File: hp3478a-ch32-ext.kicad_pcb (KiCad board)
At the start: 4 copper layers, 40 x 50 mm, 55 parts, among them J1 Conn_GPIB, J2 Pwr, J4 USB, J5 Micro_SD_Card_Det1, Q1 BSS138, SW1 RST, U1 CH32V203CxTx, U2 TLV76701DRVx, U3 AHT20, Y1 24MHz, 10pF

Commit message: chore: upd
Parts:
- R1: value 430k -> 470k
- R2: value 82k -> 150k

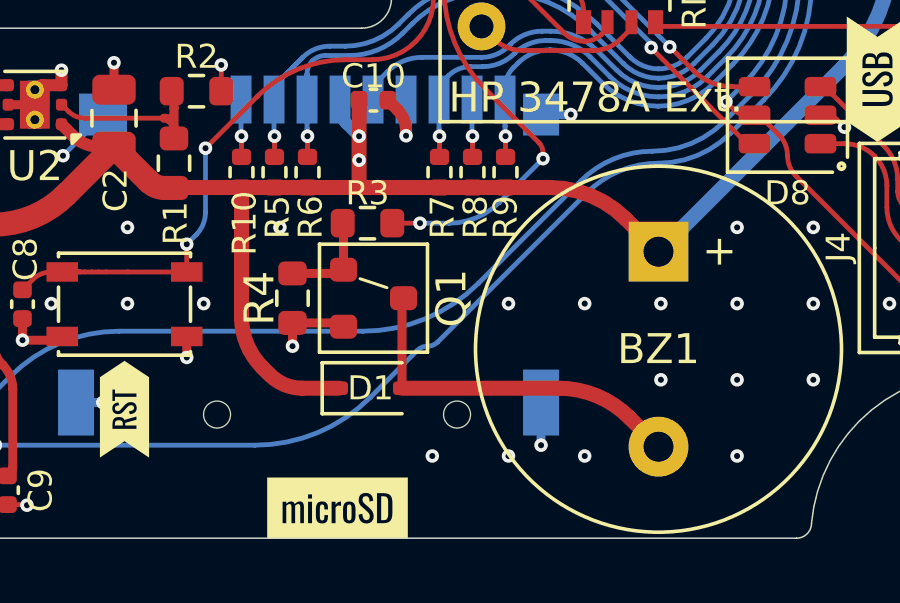
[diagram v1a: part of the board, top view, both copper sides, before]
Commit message: fix: hole clearance
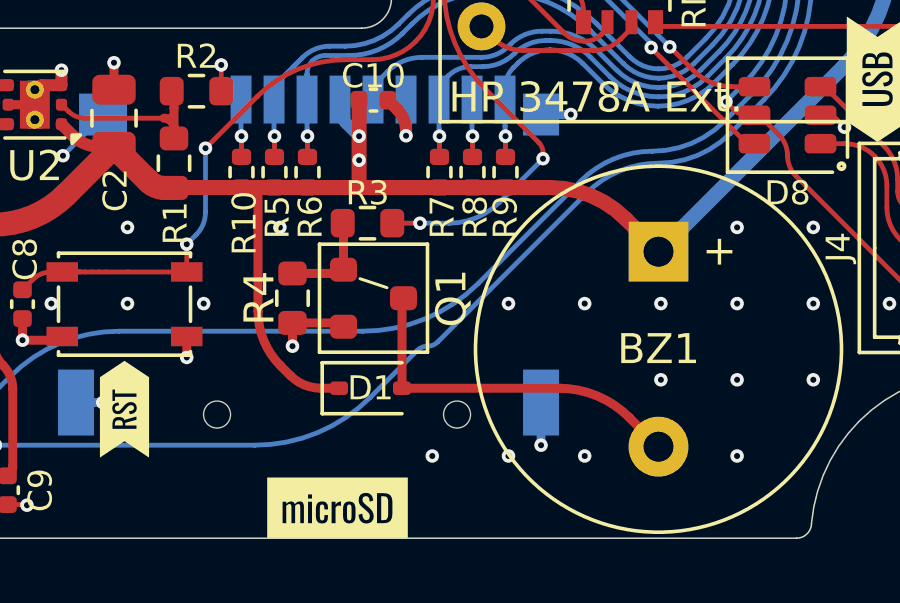
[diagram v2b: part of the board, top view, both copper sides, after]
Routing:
- net VDD: track 141.5 -> 140.9 mm

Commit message: zz
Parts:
- moved kibuzzard-68A1C101 6.52 mm to (33.6, 80.2), turned to 0 degrees
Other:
- board text added: "Rev: 2"
